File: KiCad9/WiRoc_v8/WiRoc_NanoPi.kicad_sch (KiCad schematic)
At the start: 49 parts, among them J1 Conn_02x05_Odd_Even, J10 Conn_01x09_Socket, J2 Conn_01x04, J5 Conn_01x04_Socket, J6 HAT_Conn_DBG, J8 Conn_01x06, SW1 SW_SPST, U2 OLED, U3 AXP209, U5 SY6280, U6 BatteryPadM, U7 BatteryPadP

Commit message: etc
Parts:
- removed C15: 47uF, Capacitor_SMD:C_1206_3216Metric, symbol Device:C
- added R6: 3.6K-1%, Resistor_SMD:R_0402_1005Metric, symbol Device:R
- added U1: SY6280, Package_TO_SOT_SMD:SOT-23-5, symbol WiRoc:SY6280
- C1, C10, C11, C3, C8: LCSC Part # C19666 -> C23733; ManufacturerPartNumber CL10A475KO8NNNC -> CL05A475MP5NRNC
- C14, C4, C5: LCSC Part # C19702 -> C15525; ManufacturerPartNumber CL10A106KP8NNNC -> CL05A106MQ5NUNC
- C16, C2, C25, C6, C9: LCSC Part # C15849 -> C52923; ManufacturerPartNumber CL10A105KB8NNNC -> CL05A105KA5NQNC
- C17: value 47uF -> 10uF; footprint Capacitor_SMD:C_1206_3216Metric -> Capacitor_SMD:C_0402_1005Metric; LCSC Part # C96123 -> C15525; Manufacturer Murata Electronics -> Samsung Electro-Mechanics; ManufacturerPartNumber CL31A476MPHNNNE -> CL05A106MQ5NUNC; Package 1206 -> 0603; WebsiteURL (none) -> https://lcsc.com/product-detail/Multilayer-Ceramic-Capacito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
- C26, C27: footprint Capacitor_SMD:C_0402_1005Metric -> Capacitor_SMD:C_0603_1608Metric
- C7: value 100pF -> 1uF; LCSC Part # C14858 -> C52923; ManufacturerPartNumber CL10C101JB8NNNC -> CL05A105KA5NQNC
- U10: value ~ -> SY7069ADC
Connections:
- net GND: now also C17.2, R6.1, U1.2 (GND); no longer C17.1
- net SRR_NRST: now also J2.4 (Pin_4), U1.4 (EN); no longer J8.3 (Pin_3)
- net VDD_5V: no longer C17.2
- net VDD_SYS_3.3V: now also U1.5 (IN); no longer J1.1 (Pin_1), J2.4 (Pin_4)
- new net: R6.2, U1.3 (ISET)
- new net: C17.1, J1.1 (Pin_1), J8.3 (Pin_3), U1.1 (OUT)
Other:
- moved on the sheet: J5, J6, U2

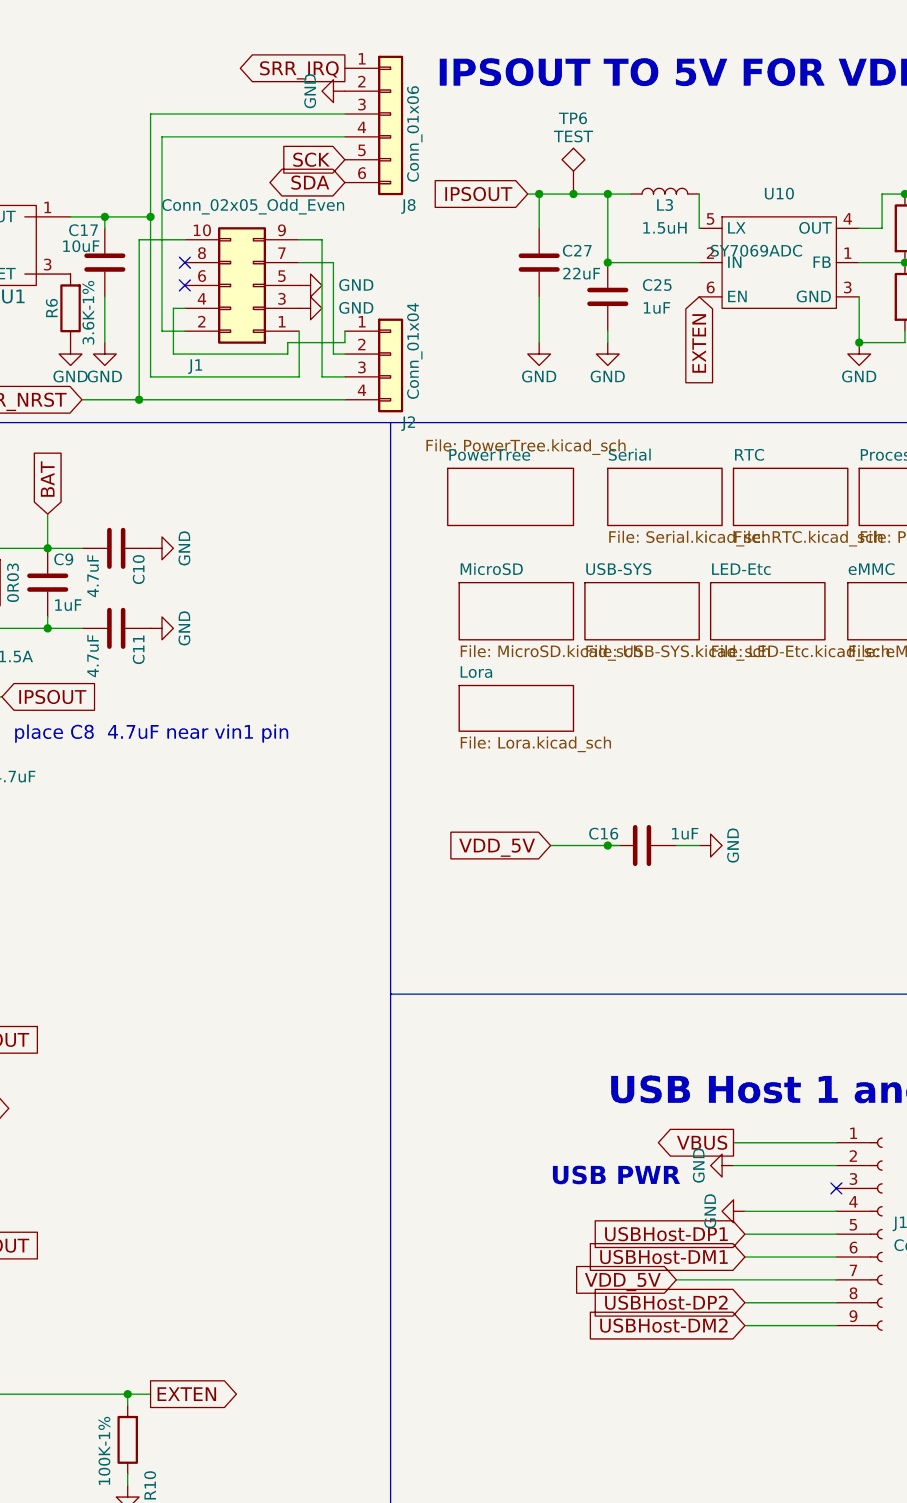
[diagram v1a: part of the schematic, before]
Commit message: more routing of WiRoc_v8, upgraded USBConnectorPlate to v9 and with ferrit beads, added an ESPHosted testboard
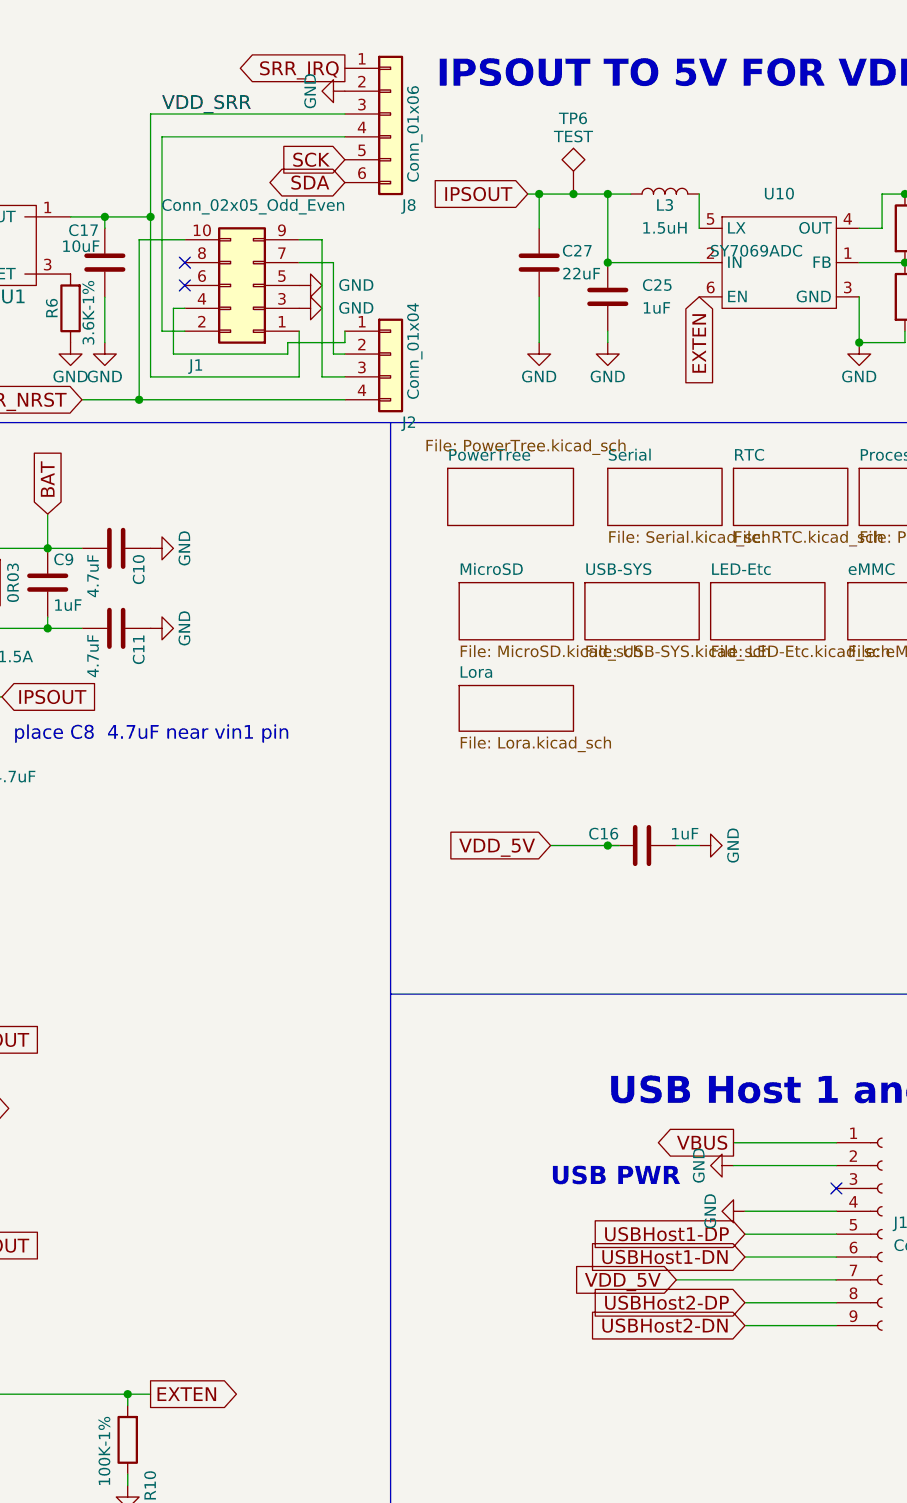
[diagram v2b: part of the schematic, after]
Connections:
- net VDD_SRR: now reaches C17.1, J1.1 (Pin_1), J8.3 (Pin_3), U1.1 (OUT)
- net USBHost-DM1 renamed USBHost1-DN
- net USBHost-DM2 renamed USBHost2-DN
- net USBHost-DP1 renamed USBHost1-DP
- net USBHost-DP2 renamed USBHost2-DP
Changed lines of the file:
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@@
+		)
+	)
+	(label "VDD_SRR"
+		(at 134.62 19.05 0)
+		(effects
+			(font
+				(size 1.524 1.524)
+			)
+			(justify left bottom)
 		)
 	)
@@
 		)
 	)
-	(global_label "USBHost-DP2"
+	(global_label "USBHost2-DP"
 		(shape input)
 		(at 199.39 151.13 180)
@@
 		)
 		(property "Intersheetrefs" "${INTERSHEET_REFS}"
-			(at 180.6502 151.13 0)
+			(at 180.5548 151.13 0)
 			(effects
 				(font
@@
 		)
 	)
-	(global_label "USBHost-DP1"
+	(global_label "USBHost1-DP"
 		(shape input)
 		(at 199.39 143.51 180)
@@
 		)
 		(property "Intersheetrefs" "${INTERSHEET_REFS}"
-			(at 180.6502 143.51 0)
-			(effects
-				(font
-					(size 1.27 1.27)
-				)
-				(justify right)
-				(hide yes)
-			)
-		)
-	)
-	(global_label "USBHost-DM2"
+			(at 180.5548 143.51 0)
+			(effects
+				(font
+					(size 1.27 1.27)
+				)
+				(justify right)
+				(hide yes)
+			)
+		)
+	)
+	(global_label "USBHost2-DN"
 		(shape input)
 		(at 199.39 153.67 180)
@@
 		)
 		(property "Intersheetrefs" "${INTERSHEET_REFS}"
-			(at 180.4325 153.67 0)
+			(at 180.4822 153.67 0)
 			(effects
 				(font
@@
 		)
 	)
-	(global_label "USBHost-DM1"
+	(global_label "USBHost1-DN"
 		(shape input)
 		(at 199.39 146.05 180)
@@
 		)
 		(property "Intersheetrefs" "${INTERSHEET_REFS}"
-			(at 180.4325 146.05 0)
-			(effects
-				(font
+			(at 180.4822 146.05 0)
+			(effects
+				(font

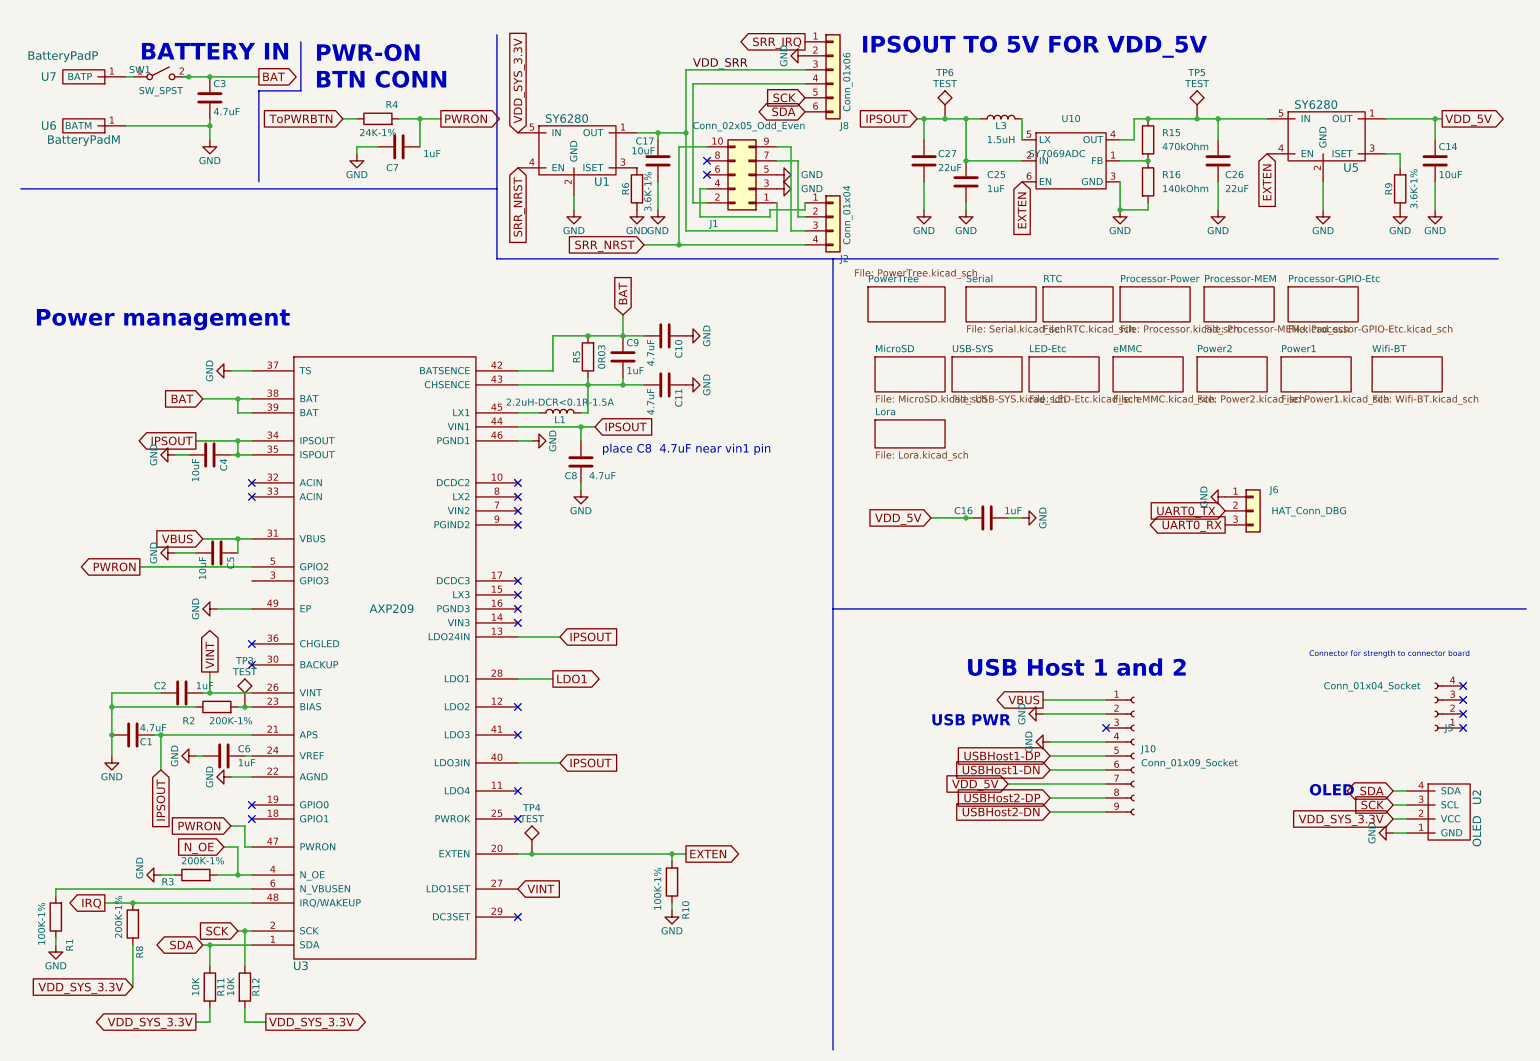
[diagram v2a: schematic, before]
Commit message: add bom
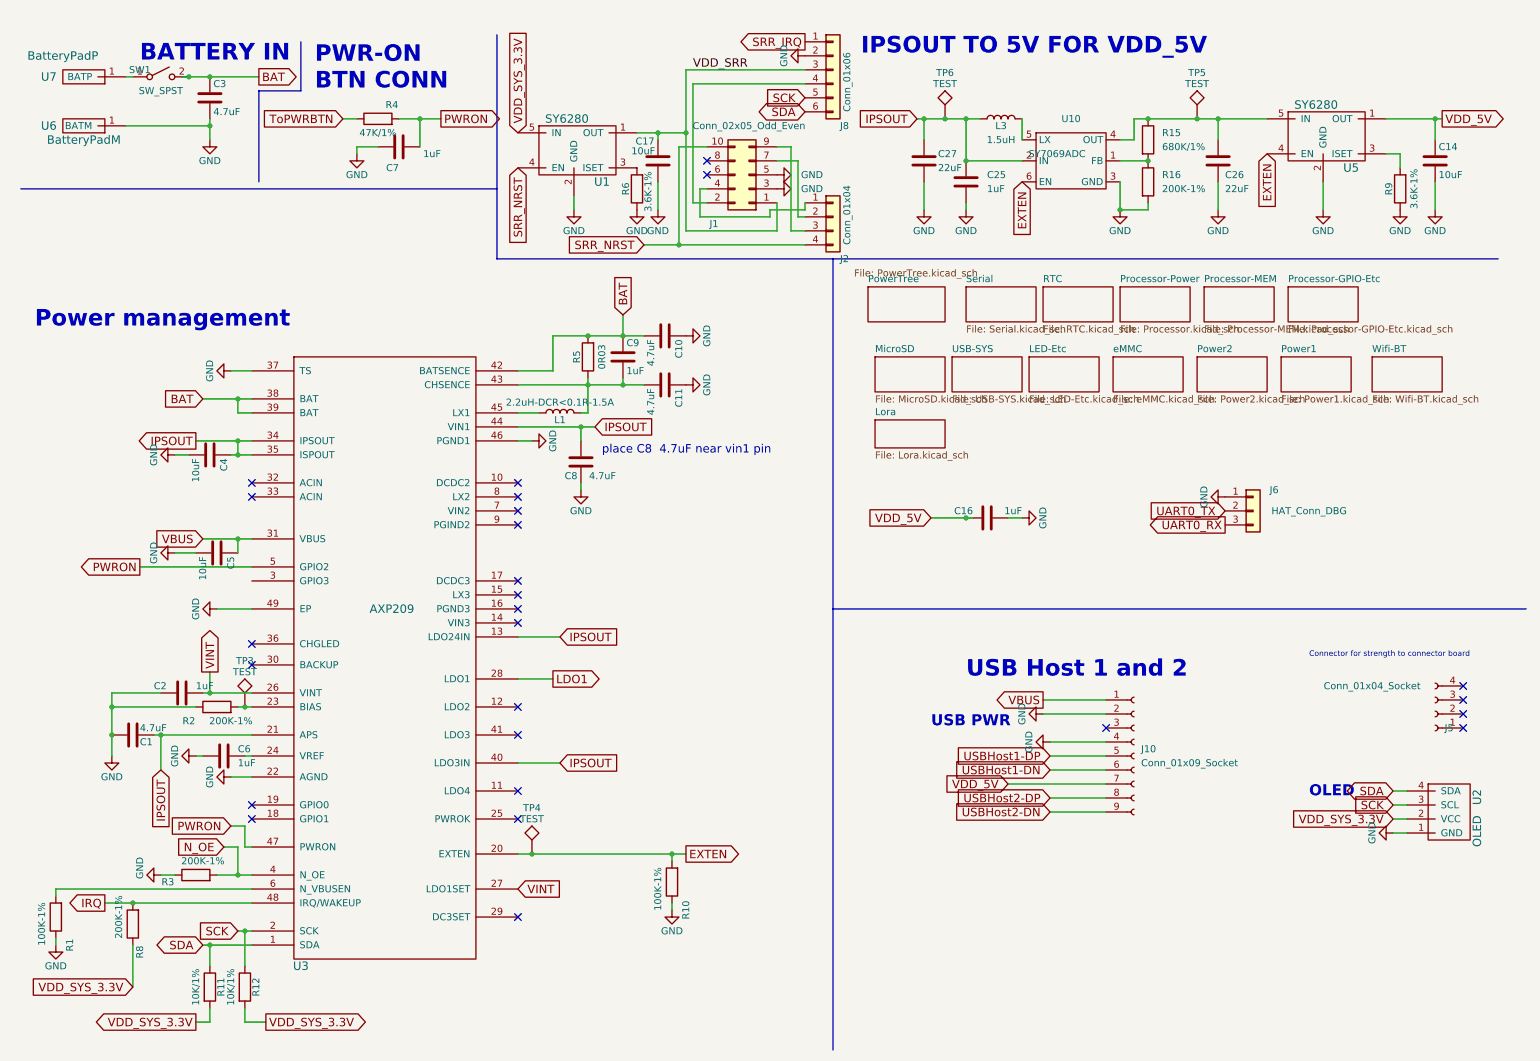
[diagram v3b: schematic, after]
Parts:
- C1, C10, C11, C14, C16, C17, C2, C25, C3, C4, C5, C6, C7, C8, C9: JLCBasicExtended (none) -> Basic; Package 0603 -> 0402
- C26, C27: JLCBasicExtended (none) -> Extended; Manufacturer (none) -> Murata Electronics; ManufacturerPartNumber (none) -> GRM188R61A226ME15D; Note (none) -> Selected this one due to the small package size; Package (none) -> 0603; PartNo GRM188R61A226ME15D -> (none)
- J1: IncludeInBOM (none) -> FALSE; JLCBasicExtended (none) -> Extended; LCSC Part # (none) -> C5142394; Manufacturer (none) -> MINTRON; ManufacturerPartNumber (none) -> MTP310-1205S2
- J10: JLCBasicExtended (none) -> Extended; LCSC Part # (none) -> C17700136; Manufacturer (none) -> XFCN; ManufacturerPartNumber (none) -> PM127V-11-09-H46
- J5: JLCBasicExtended (none) -> Extended; LCSC Part # (none) -> C17700132; Manufacturer (none) -> XFCN; ManufacturerPartNumber (none) -> PM127V-11-04-H46
- L1, U1, U3, U5: JLCBasicExtended (none) -> Extended
- L3: JLCBasicExtended (none) -> Extended; Package SMD -> (none); PartNo SLW4020S1R5MST -> (none)
- R1, R10: JLCBasicExtended (none) -> Basic; LCSC Part # C25803 -> C25741; ManufacturerPartNumber 0603WAF1003T5E -> 0402WGF1003TCE; Package 0603 -> 0402
- R11, R12: value 10K -> 10K/1%; JLCBasicExtended (none) -> Basic; LCSC Part # C25804 -> C25744; ManufacturerPartNumber 0603WAF1002T5E -> 0402WGF1002TCE; Package 0603 -> 0402
- R15: value 470kOhm -> 680K/1%; JLCBasicExtended (none) -> Extended; LCSC Part # C23178 -> C4131; Manufacturer (none) -> Uniroyal Elec; ManufacturerPartNumber HPCR0603F470KK9 -> 0402WGF6803TCE; Package (none) -> 0402; PartNo HPCR0603F470KK9 -> (none)
- R16: value 140kOhm -> 200K-1%; JLCBasicExtended (none) -> Basic; LCSC Part # C321721 -> C25764; Manufacturer (none) -> Uniroyal Elec; ManufacturerPartNumber 0603WAF140KT5E -> 0402WGF2003TCE; Package (none) -> 0402; PartNo 0603WAF140KT5E -> (none)
- R2, R3, R8: JLCBasicExtended (none) -> Basic; LCSC Part # C25811 -> C25764; ManufacturerPartNumber 0603WAF2003T5E -> 0402WGF2003TCE; Package 0603 -> 0402
- R4: value 24K-1% -> 47K/1%; JLCBasicExtended (none) -> Basic; LCSC Part # C23352 -> C25792; ManufacturerPartNumber 0603WAF2402T5E -> 0402WGF4702TCE; Package 0603 -> 0402
- R5: JLCBasicExtended (none) -> Basic
- R6, R9: footprint Resistor_SMD:R_0402_1005Metric -> Resistor_SMD:R_0603_1608Metric; JLCBasicExtended (none) -> Basic
- U10: JLCBasicExtended (none) -> Extended; Package (none) -> TSOT-23-6

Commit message: change tracewidth for mem, add nettie for better length calculation
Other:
- title: WiRoc NanoPI Hat -> WiRoc
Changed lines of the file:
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@@
 	(paper "A4")
 	(title_block
-		(title "WiRoc NanoPI Hat")
+		(title "WiRoc")
 		(date "2018-03-31")
 		(rev "1")
